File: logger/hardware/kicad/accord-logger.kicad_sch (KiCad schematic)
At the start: 91 parts, among them J1 Power 2-way, J2 Cluster harness 8-way, J3 Bus / expansion (unpopulated), J4 Service 4-way, J5 SD breakout 6-way, Q1 IRF4905PbF, Q2 2N3904, Q3 2N3904, U1 RaspberryPi_Pico_W, U2 PC817, U3 LM2678T-5.0, X1 SIGNAL_ISOLATION (required), X2 SIGNAL_ISOLATION (under revie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, X3 SIGNAL_ISOLATION (under revie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, X4 SIGNAL_ISOLATION (under revie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, X5 SIGNAL_ISOLATION (under revie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, X6 IGN_QUALIFICATION, X7 VEHICLE_PROTECTION, X8 MAX_ON

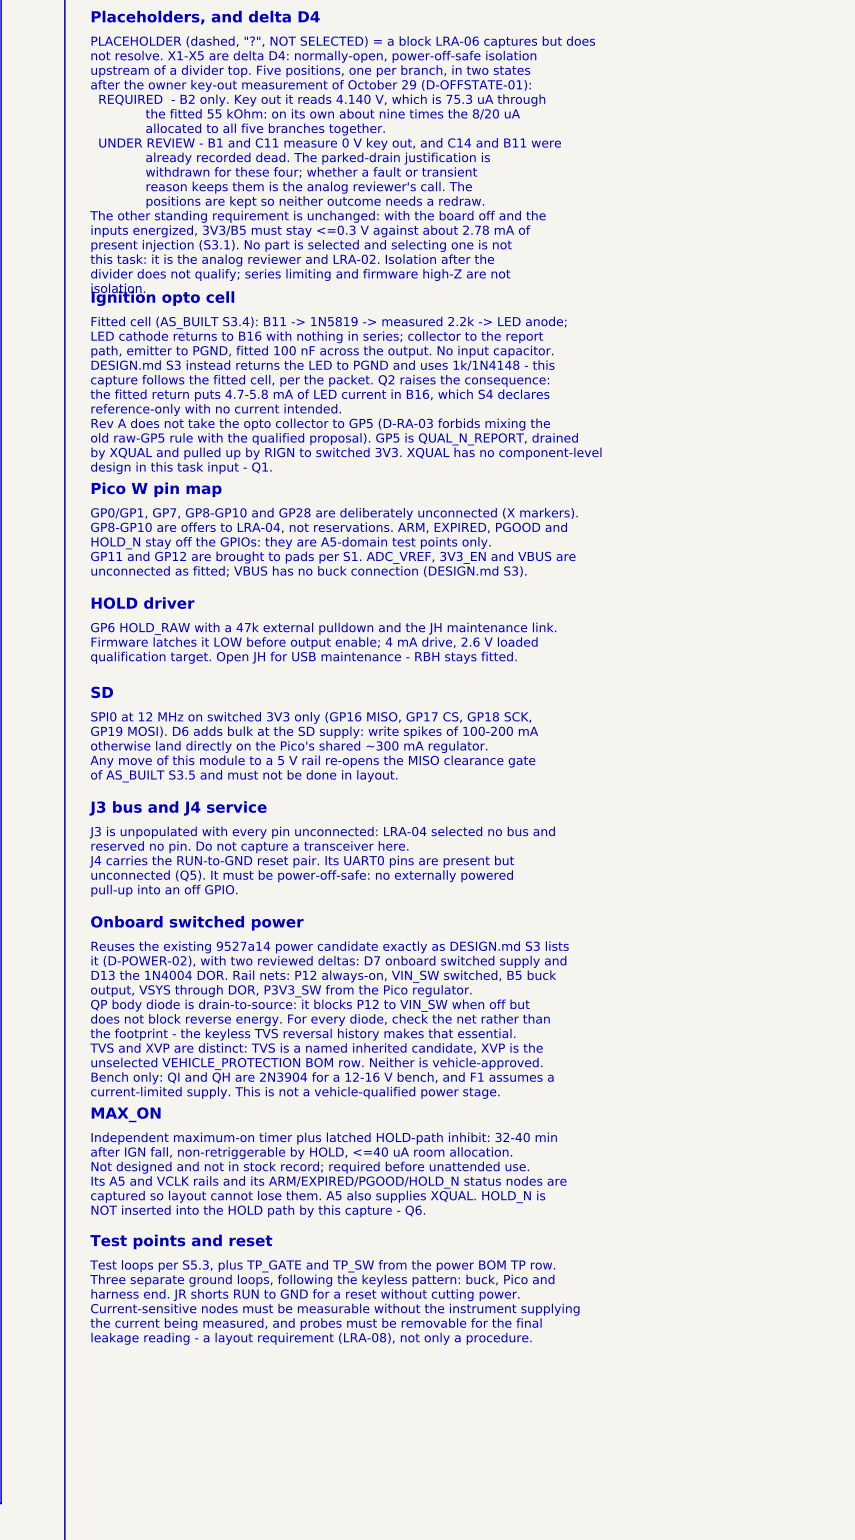
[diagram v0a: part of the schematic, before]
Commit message: logger-schematic: correct the B2 isolation annotation to the measured back-feed
The B2 D4 annotation carried two figures that the owner's configuration
clarification superseded. Every VSS reading was taken with the dividers,
clamps, Pico module and SD module seated and only the USB lead pulled, so
the clamp conducts and the divider was never the only load.

Corrected, following AS_BUILT U-08/U-10/U-14 and REV_A_INTERFACES D4 at
9b24eda:

- B2 draws 134-141 uA, not 75.3 uA, at 4.140 V loaded against 4.669 V
  open-circuit.
- 99-110 uA of that is back-fed into the Pico's unpowered 3V3 rail through
  a forward-biased clamp, measured at 0.883 V on the clamp cathodes.
- One branch alone exceeds the 100 uA whole-system parked budget, against
  an 8/20 uA allocation for all five.
- B2's parked source is 3.8-3.9 kOhm, not 7.03 kOhm.

The annotation now states this as a back-feed path rather than only a
drain, and records that it is the one row of REV_A_INTERFACES section 6's
off-state matrix established by measurement. The superseded 75.3 uA and
7.03 kOhm appear nowhere in the drawing, BOM or symbol library; the capture
notes name them once, as figures not to reintroduce.

X1 stays required and X2-X5 stay under analog review, unchanged. No part
selected, no ratio or pin changed, no placeholder promoted or removed.

kicad-cli 9.0.2 ERC remains 0 violations at --severity-all, SVG and netlist
export clean, and the 201 netlist/BOM checks still pass.

Agent-Session: logger-schematic
Claude-Session-ID: 73d7d954-f82a-4038-8ff3-546a23fc5fa9
Co-Authored-By: Claude Opus 5 <noreply@anthropic.com>
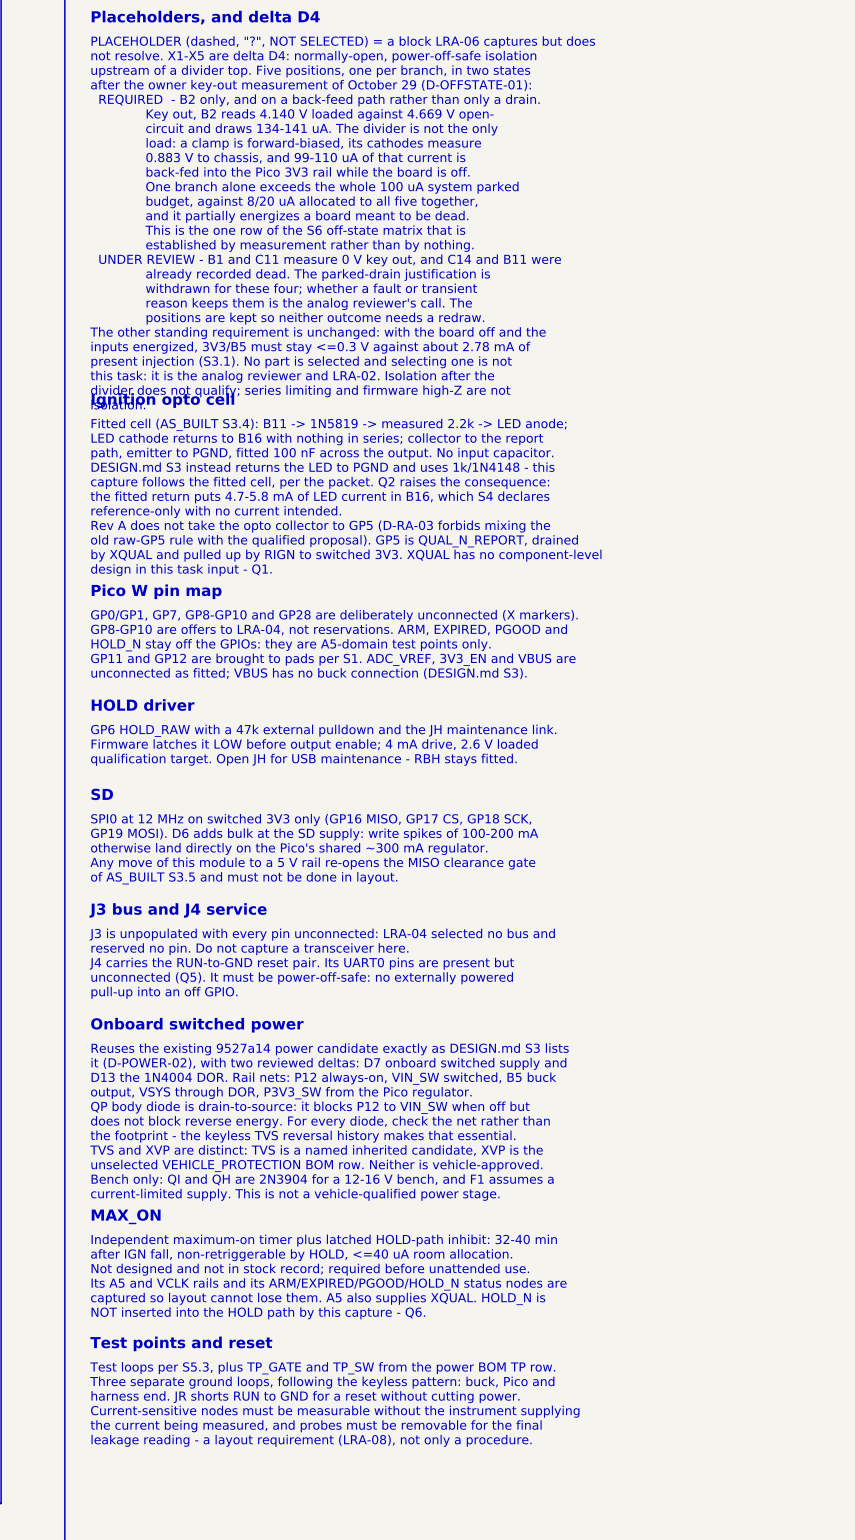
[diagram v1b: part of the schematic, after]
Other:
- note added: "PLACEHOLDER (dashed, "?", NOT SELECTED) = a block LRA-06 captures but does not resolve. X1-X5 are delta D4: normally-open, power-off-safe isolation upstream of a divider top. Five positions, one per branch, in two states after the owner key-out measurement of October 29 (D-OFFSTATE-01): REQUIRED - B2 only, and on a back-feed path rather than only a drain. Key out, B2 reads 4.140 V loaded against 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"
- note removed: "PLACEHOLDER (dashed, "?", NOT SELECTED) = a block LRA-06 captures but does not resolve. X1-X5 are delta D4: normally-open, power-off-safe isolation upstream of a divider top. Five positions, one per branch, in two states after the owner key-out measurement of October 29 (D-OFFSTATE-01): REQUIRED - B2 only. Key out it reads 4.140 V, which is 75.3 uA through the fitted 55 kOhm: on its own about nin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"

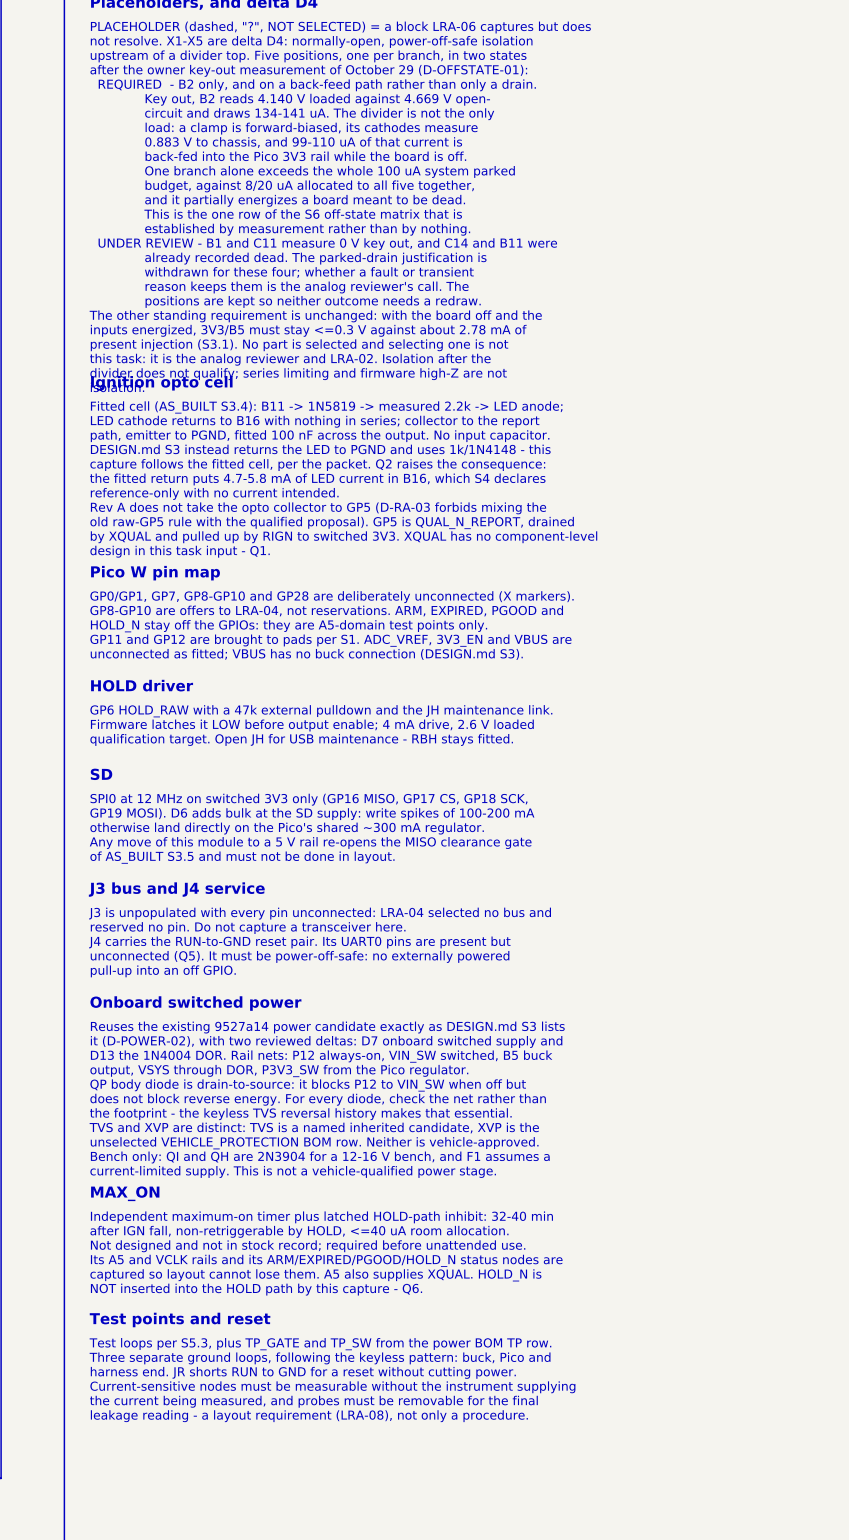
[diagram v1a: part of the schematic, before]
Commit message: logger-schematic: put the exact B2 figures on the drawing, and point at U-07
The owner's 22k/33k junction reading removed the last assumption behind the
B2 annotation, so the ranges are replaced with the measured values from
AS_BUILT U-07/U-08/U-14 and REV_A_INTERFACES D4 at bcac2e7:

- 140.8 uA drawn, was 134-141.
- 109.2 uA back-fed into the Pico's unpowered 3V3 rail through the forward-
  biased clamp, was 99-110; only 31.6 uA reaches ground through the 33k.
- Parked source 3,757 ohm, was 3.8-3.9 kOhm.
- One branch is 141 percent of the whole 100 uA system parked budget and
  17.6x the 8 uA allocated to all five.

The four readings that fix it with nothing estimated are on the drawing and
tabulated in the capture notes: 4.669 V open-circuit, 4.140 V loaded at the
tap, 1.042 V at the junction, 0.883 V on the clamp cathodes.

The superseded-figures list in CAPTURE_NOTES is now a table of five entries,
each with the assumption that made it wrong. The three new entries share one
cause: a clamp forward drop bracketed between 0.15 V and 0.30 V, which the
junction reading measured.

Also recorded, as a pointer rather than an action: the same readings give the
B2 clamp 159 mV at 109 uA at room temperature, which is U-07's first measured
point and a Schottky drop corroborating the reported 1N5819. It cuts against
D11, since V_F falls further below that current, so the tach cell's clamp
onset is lower and its margin smaller than estimated. The B2 clamp and the
X2 placeholder each carry the pointer. D11 is not LRA-06's and nothing here
acts on it.

X1 stays required, X2-X5 stay under analog review. No part selected, no ratio
or pin changed, no placeholder promoted or removed.

kicad-cli 9.0.2 ERC remains 0 violations at --severity-all, SVG and netlist
export clean, and the 201 netlist/BOM checks still pass.

Agent-Session: logger-schematic
Claude-Session-ID: 73d7d954-f82a-4038-8ff3-546a23fc5fa9
Co-Authored-By: Claude Opus 5 <noreply@anthropic.com>
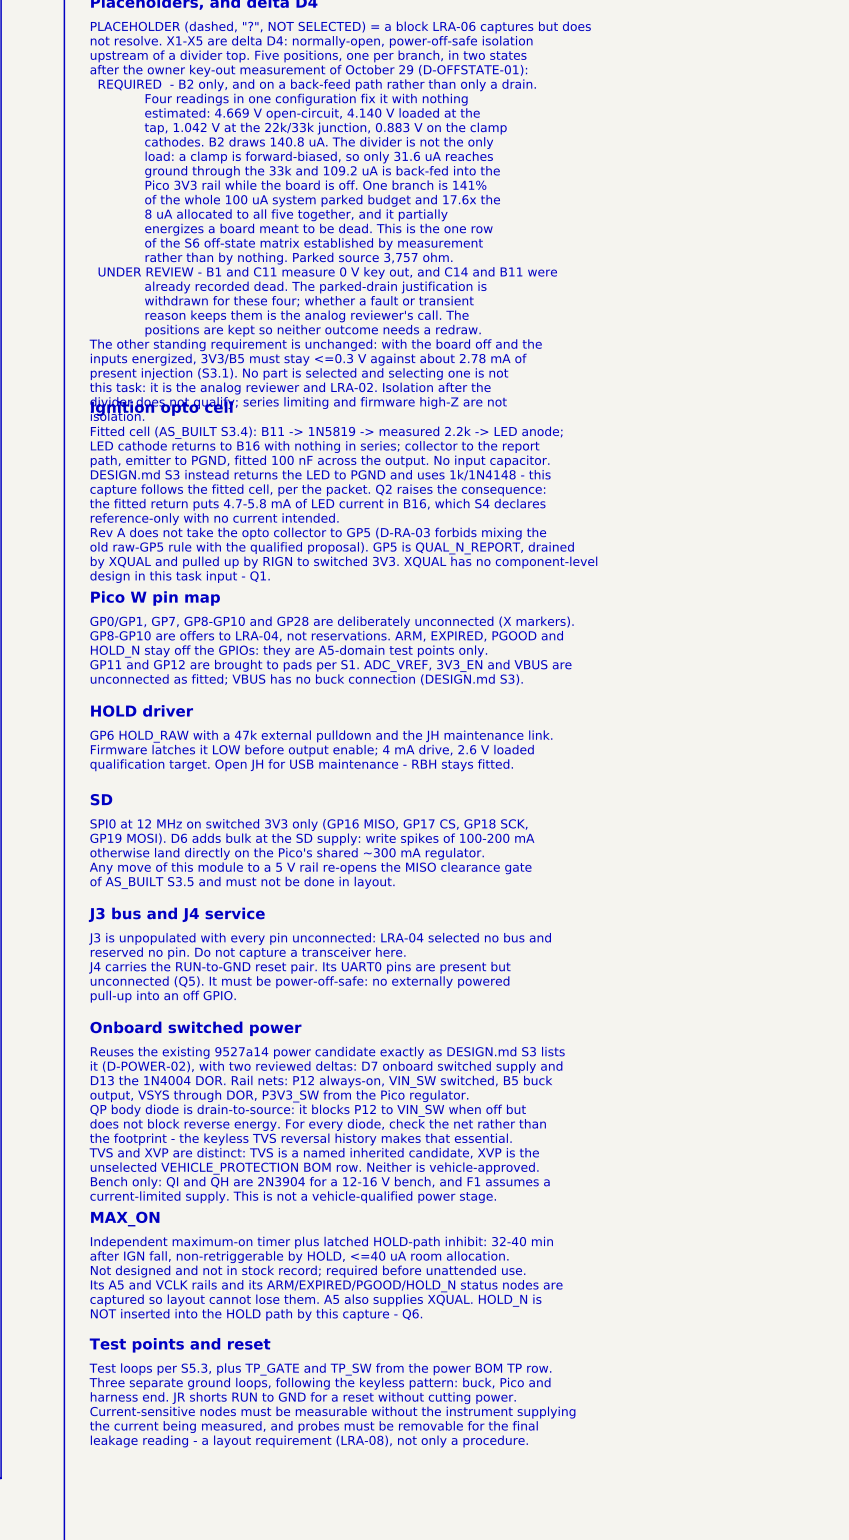
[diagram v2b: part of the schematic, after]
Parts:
- D101, D102, D103: Source AS_BUILT S2/S3.4a -> AS_BUILT S2/S3.4a, U-07
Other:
- note added: "PLACEHOLDER (dashed, "?", NOT SELECTED) = a block LRA-06 captures but does not resolve. X1-X5 are delta D4: normally-open, power-off-safe isolation upstream of a divider top. Five positions, one per branch, in two states after the owner key-out measurement of October 29 (D-OFFSTATE-01): REQUIRED - B2 only, and on a back-feed path rather than only a drain. Four readings in one configuration fix it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"
- note removed: "PLACEHOLDER (dashed, "?", NOT SELECTED) = a block LRA-06 captures but does not resolve. X1-X5 are delta D4: normally-open, power-off-safe isolation upstream of a divider top. Five positions, one per branch, in two states after the owner key-out measurement of October 29 (D-OFFSTATE-01): REQUIRED - B2 only, and on a back-feed path rather than only a drain. Key out, B2 reads 4.140 V loaded against 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"

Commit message: logger-schematic: bond the cluster ground sense to the single ADC return
Applies review findings R06-REV-1 (blocking) and R06-REV-3 (minor) from
coordination/reviews/LRA06_REVIEW_2026-10-29.md.

R06-REV-1. J2.6, the B16 cluster ground-sense conductor, was left on a net
of its own containing only itself and the optocoupler LED cathode. It never
joined the node carrying both ADC divider bottoms, their filter and clamp
returns and the Pico's AGND pin, so both ADC channels referenced local
analog ground and any cluster-to-logger offset landed uncorrected in the
fuel and supply readings. That is the error B16 exists to prevent, and it
contradicted AS_BUILT section 2 row 8, REV_A_INTERFACES section 4 and delta
D5 at once. It was an omission, not a disagreement: the capture already
treated that node as the B16 sense node, including where it placed
TP_GND_HARNESS.

J2.6 is now bonded to it at one point. The node carries ten members:
J2.6, U1.33, both divider bottoms, both filter capacitors, both lower
clamps, TP18 and the opto LED cathode.

The verification script shared the same misreading and so passed the
defective capture. Asserting that B16 was its own net was itself the bug.
It now asserts the single node's membership, member by member, which is
what section 4 and D5 actually require.

R06-REV-2 is deliberately not acted on. Bonding B16 is what sharpens it:
4.7-5.8 mA of opto LED current now flows in the node both ADC channels
reference whenever the engine runs, so D5 and the fitted LED return cannot
both stand. That is the electrical lead's decision. The LED is left where
the as-built puts it, and the drawing, the BOM and CAPTURE_NOTES question
Q2 each state the consequence.

R06-REV-3. ADC_VREF's unconnected state is now dispositioned in writing as
CAPTURE_NOTES question Q8: the pin is the module's own filtered reference
output, nothing is fitted there in the as-built, and it carries an explicit
no-connect. No change to the drawing.

accord-logger.kicad_pro is KiCad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
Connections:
- net B16 is gone; now on net AGND: J2.6 (Pin_6), U2.2
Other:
- note added: "Five fitted cells, carried forward with no value changed (AS_BUILT S2). Digital divider bottoms return to PGND. Both ADC divider bottoms, their filter and clamp returns, J2.6 (the B16 cluster ground sense) and Pico AGND are ONE node, bonded at a single point (S4, delta D5, R06-REV-1). Layout must not create a second path to it. B16 must never become a power return - but the fitted opto LED return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"
- note removed: "Five fitted cells, carried forward with no value changed (AS_BUILT S2). Digital divider bottoms return to PGND; both ADC divider bottoms and the B16 cluster sense land on ONE common node, then Pico AGND (S4, delta D5). B16 must never become a power return: see the ignition note and Q2/Q7. Both ADC channels already carry 1k + 1uF + two 1N5819 - fitted, not new (D3 closed)."
